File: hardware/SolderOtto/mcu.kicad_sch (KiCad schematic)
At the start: 30 parts, among them J301 TC-2050, P301 USB_C_Plug_USB2.0, SW301 SW_Push, U301 USBLC6-2SC6, U302 STM32G474QETx, U303 MX25R3235FM1xx0, Y301 32.768 kHz

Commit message: fix some part numbers
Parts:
- C317, C318: Digikey (none) -> 311-1636-1-ND
- R301, R302: Digikey (none) -> RMCF0603ZT0R00CT-ND
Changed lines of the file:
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@@
+			)
+		)
+		(property "Digikey" "311-1636-1-ND"
+			(at 304.8 232.41 0)
+			(effects
+				(font
+					(size 1.27 1.27)
+				)
+				(hide yes)
 			)
 		)
@@
 			)
 		)
+		(property "Digikey" "RMCF0603ZT0R00CT-ND"
+			(at 67.31 69.85 90)
+			(effects
+				(font
+					(size 1.27 1.27)
+				)
+				(hide yes)
+			)
+		)
 		(pin "1"
 		)
@@
 			)
 		)
+		(property "Digikey" "311-1636-1-ND"
+			(at 288.29 232.41 0)
+			(effects
+				(font
+					(size 1.27 1.27)
+				)
+				(hide yes)
+			)
+		)
 		(pin "1"
 		)
@@
 			(effects
 				(font
+					(size 1.27 1.27)
+				)
+				(hide yes)
+			)
+		)
+		(property "Digikey" "RMCF0603ZT0R00CT-ND"
+			(at 67.31 67.31 90)
+			(effects
+				(font

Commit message: remove low side switching ic
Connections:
- net Channel0_LOW_SIDE_COM: now reaches U302.32 (PA3)
- net Channel0_LOW_SIDE_SW renamed Channel0_LOW_SIDE_LOAD
- no-connect marks 17 -> 16
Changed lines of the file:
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@@
 	)
 	(no_connect
-		(at 212.09 67.31)
-	)
-	(no_connect
 		(at 161.29 107.95)
 	)
@@
 	(wire
 		(pts
+			(xy 212.09 67.31) (xy 228.6 67.31)
+		)
+		(stroke
+			(width 0)
+			(type default)
+		)
+	)
+	(wire
+		(pts
 			(xy 189.23 232.41) (xy 189.23 234.95)
 		)
@@
 		)
 	)
-	(hierarchical_label "Channel0_LOW_SIDE_SW"
+	(hierarchical_label "Channel0_LOW_SIDE_LOAD"
 		(shape output)
 		(at 143.51 102.87 180)
@@
 		)
 	)
+	(hierarchical_label "Channel0_LOW_SIDE_COM"
+		(shape output)
+		(at 228.6 67.31 0)
+		(fields_autoplaced yes)
+		(effects
+			(font
+				(size 1.27 1.27)
+			)
+			(justify left)
+		)
+	)

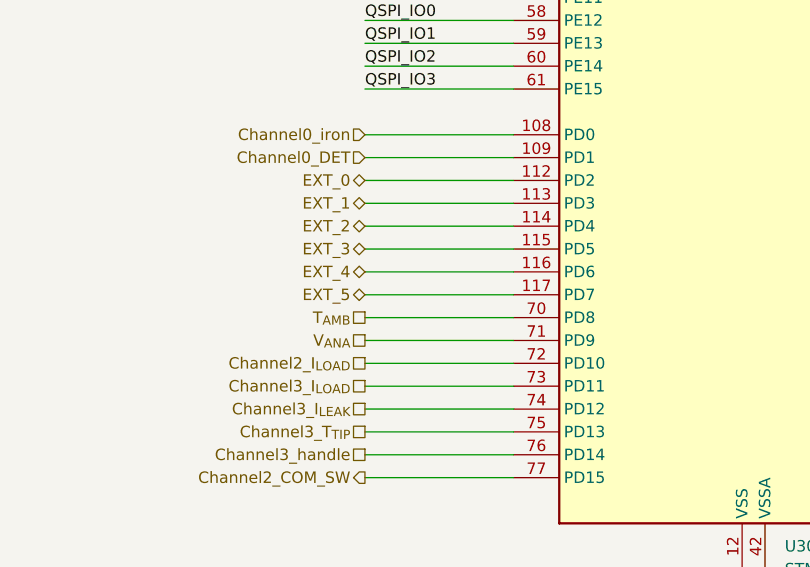
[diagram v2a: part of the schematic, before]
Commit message: rework pcb due to not working one
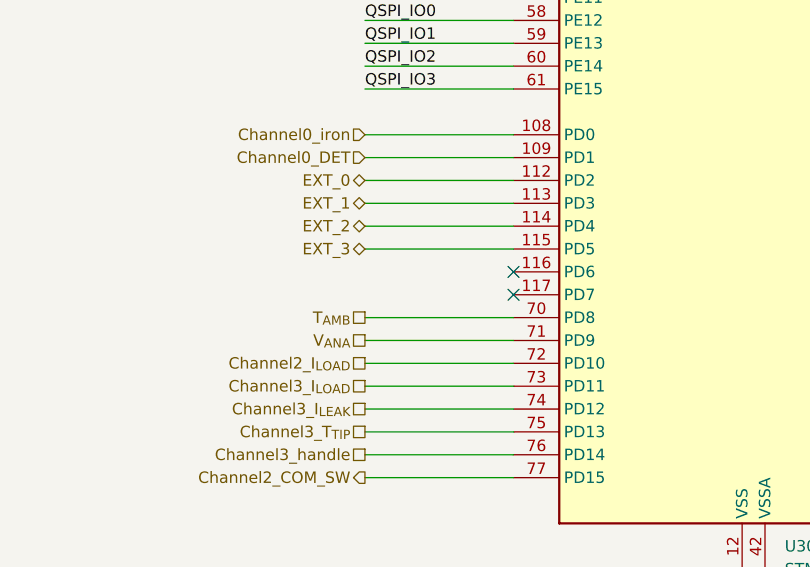
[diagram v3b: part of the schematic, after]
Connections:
- net EXT_4: no longer names the net of U302.116 (PD6)
- net EXT_5: no longer names the net of U302.117 (PD7)
- no-connect marks 16 -> 18
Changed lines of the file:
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@@
 	)
 	(no_connect
+		(at 161.29 199.39)
+	)
+	(no_connect
 		(at 212.09 176.53)
 	)
@@
 		(at 53.34 248.92)
 	)
+	(no_connect
+		(at 161.29 201.93)
+	)
 	(wire
 		(pts
@@
 	(wire
 		(pts
-			(xy 144.78 201.93) (xy 161.29 201.93)
-		)
-		(stroke
-			(width 0)
-			(type default)
-		)
-	)
-	(wire
-		(pts
 			(xy 144.78 118.11) (xy 161.29 118.11)
 		)
@@
 	(wire
 		(pts
-			(xy 144.78 199.39) (xy 161.29 199.39)
-		)
-		(stroke
-			(width 0)
-			(type default)
-		)
-	)
-	(wire
-		(pts
 			(xy 378.46 76.2) (xy 378.46 78.74)
 		)
@@
 		)
 	)
-	(hierarchical_label "EXT_5"
-		(shape bidirectional)
-		(at 144.78 201.93 180)
-		(fields_autoplaced yes)
-		(effects
-			(font
-				(size 1.27 1.27)
-			)
-			(justify right)
-		)
-	)
 	(hierarchical_label "Channel2_handle"
 		(shape passive)
@@
 		)
 	)
-	(hierarchical_label "EXT_4"
-		(shape bidirectional)
-		(at 144.78 199.39 180)
-		(fields_autoplaced yes)
-		(effects
-			(font
-				(size 1.27 1.27)
-			)
-			(justify right)
-		)
-	)

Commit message: rework pcb
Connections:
- net Channel3_SEL1 is gone; now on net ZCD: U302.83 (PG1)
- net Buzzer: now also U302.97 (PF6); no longer U302.7 (PC13)
- net Channel0_COM_SW: now also U302.14 (PF5); no longer U302.27 (PA0)
- net Channel0_I_{LEAK}: now also U302.27 (PA0); no longer U302.25 (PC3)
- net Channel0_LOAD0_SW: now also U302.7 (PC13); no longer U302.28 (PA1)
- net Channel0_LOAD1_SW: now also U302.11 (PF4); no longer U302.29 (PA2)
- net Channel0_LOW_SIDE_COM: now also U302.10 (PF3); no longer U302.32 (PA3)
- net Channel0_LOW_SIDE_LOAD: now also U302.15 (PF7); no longer U302.26 (PF2)
- net Channel0_iron: now also U302.36 (PA7); no longer U302.108 (PD0)
- net Channel0_stand: now also U302.35 (PA6); no longer U302.66 (PB12)
- net Channel0_tip: now also U302.34 (PA5); no longer U302.103 (PG5)
- net Channel1_COM_SW: no longer U302.41 (PB2)
- net Channel1_I_{LEAK}: no longer U302.35 (PA6)
- net Channel1_I_{LOAD}: no longer U302.36 (PA7)
- net Channel1_LOAD0_SW: no longer U302.39 (PB0)
- net Channel1_LOAD1_SW: no longer U302.40 (PB1)
- net Channel1_LOW_SIDE_SW: no longer U302.38 (PC5)
- net Channel1_T_{TIP}: no longer U302.34 (PA5)
- net Channel1_handle: no longer U302.33 (PA4)
- net Channel1_iron: no longer U302.119 (PB4)
- net Channel1_stand: no longer U302.67 (PB13)
- net Channel1_tip: no longer U302.104 (PG6)
- net Channel2_COM_SW: no longer U302.77 (PD15)
- net Channel2_I_{LEAK}: no longer U302.53 (PE7)
- net Channel2_I_{LOAD}: no longer U302.72 (PD10)
- net Channel2_LOAD0_SW: no longer U302.80 (PC6)
- net Channel2_LOAD1_SW: no longer U302.81 (PC7)
- net Channel2_LOW_SIDE_SW: no longer U302.82 (PG0)
- net Channel2_T_{TIP}: no longer U302.54 (PE8)
- net Channel2_handle: no longer U302.55 (PE9)
- net Channel2_iron: no longer U302.120 (PB5)
- net Channel2_stand: no longer U302.68 (PB14)
- net Channel2_tip: no longer U302.105 (PG7)
- net Channel3_COM_SW: no longer U302.86 (PG4)
- net Channel3_I_{LEAK}: no longer U302.74 (PD12)
- net Channel3_I_{LOAD}: no longer U302.73 (PD11)
- net Channel3_LOAD0_SW: no longer U302.87 (PC8)
- net Channel3_LOAD1_SW: no longer U302.88 (PC9)
- net Channel3_LOW_SIDE_SW: no longer U302.89 (PA8)
- net Channel3_T_{TIP}: no longer U302.75 (PD13)
- net Channel3_handle: no longer U302.76 (PD14)
- net Channel3_iron: no longer U302.122 (PB7)
- net Channel3_stand: no longer U302.69 (PB15)
- net Channel3_tip: no longer U302.106 (PG8)
- net EXT_0: now also U302.99 (PA15); no longer U302.112 (PD2)
- net EXT_1: now also U302.100 (PC10); no longer U302.113 (PD3)
- net EXT_2: now also U302.101 (PC11); no longer U302.114 (PD4)
- net EXT_3: now also U302.102 (PC12); no longer U302.115 (PD5)
- net ZCD: no longer U302.125 (PE0)
- net Channel0_SEL2_{b}: now reaches U302.19 (PF0)
- net Channel0_DET: no longer names the net of U302.109 (PD1)
- net Channel0_SEL1 renamed Channel0_SEL1_{a}
- net Channel0_SEL2 renamed Channel0_SEL1_{b}
- net Channel0_SEL3 renamed Channel0_SEL2_{a}
- net Channel0_T_{TIP} renamed Channel0_T_{TIP}_{a}
- net Channel1_DET: no longer names the net of U302.107 (PG9)
- net Channel1_SEL1: no longer names the net of U302.48 (PF11)
- net Channel1_SEL2: no longer names the net of U302.49 (PF12)
- net Channel1_SEL3: no longer names the net of U302.50 (PF13)
- net Channel2_DET: no longer names the net of U302.121 (PB6)
- net Channel2_SEL1: no longer names the net of U302.62 (PB10)
- net Channel2_SEL2: no longer names the net of U302.65 (PB11)
- net Channel2_SEL3: no longer names the net of U302.52 (PF15)
- net Channel3_DET: no longer names the net of U302.124 (PB9)
- net Channel3_SEL2: no longer names the net of U302.84 (PG2)
- net Channel3_SEL3: no longer names the net of U302.85 (PG3)
- new net Channel0_T_{TIP}_{b}: U302.25 (PC3)
- no-connect marks 18 -> 60

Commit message: save work
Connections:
- net Channel0_COM_SW: now also U302.7 (PC13); no longer U302.14 (PF5)
- net Channel0_LOAD0_SW: now also U302.10 (PF3); no longer U302.7 (PC13)
- net Channel0_LOW_SIDE_COM: now also U302.14 (PF5); no longer U302.10 (PF3)
- net Channel0_T_{TIP}_{a}: now also U302.25 (PC3); no longer U302.24 (PC2)
- net Channel0_T_{TIP}_{b}: now also U302.24 (PC2); no longer U302.25 (PC3)
- net ZCD: now also U302.39 (PB0); no longer U302.83 (PG1)
- net Channel0_iron: no longer names the net of U302.36 (PA7)
- no-connect marks 60 -> 63
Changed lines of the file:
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@@
 	)
 	(no_connect
+		(at 212.09 77.47)
+	)
+	(no_connect
 		(at 144.78 184.15)
 	)
@@
 	)
 	(no_connect
+		(at 161.29 102.87)
+	)
+	(no_connect
 		(at 228.6 67.31)
 	)
@@
 	)
 	(no_connect
+		(at 161.29 100.33)
+	)
+	(no_connect
 		(at 143.51 133.35)
 	)
@@
 	)
 	(no_connect
-		(at 143.51 67.31)
+		(at 143.51 69.85)
 	)
 	(no_connect
@@
 	)
 	(no_connect
-		(at 228.6 102.87)
+		(at 143.51 67.31)
 	)
 	(no_connect
@@
 	(wire
 		(pts
-			(xy 212.09 77.47) (xy 228.6 77.47)
-		)
-		(stroke
-			(width 0)
-			(type default)
-		)
-	)
-	(wire
-		(pts
 			(xy 143.51 97.79) (xy 161.29 97.79)
 		)
@@
 	(hierarchical_label "Channel0_LOAD0_SW"
 		(shape output)
-		(at 228.6 179.07 0)
+		(at 143.51 105.41 180)
 		(fields_autoplaced yes)
 		(effects
@@
 				(size 1.27 1.27)
 			)
-			(justify left)
+			(justify right)
 		)
 	)
@@
 	(hierarchical_label "Channel0_T_{TIP}_{b}"
 		(shape passive)
-		(at 228.6 153.67 0)
+		(at 228.6 151.13 0)
 		(fields_autoplaced yes)
 		(effects
@@
 	(hierarchical_label "Channel0_COM_SW"
 		(shape output)
-		(at 143.51 110.49 180)
+		(at 228.6 179.07 0)
 		(fields_autoplaced yes)
 		(effects
@@
 				(size 1.27 1.27)
 			)
-			(justify right)
+			(justify left)
 		)
 	)
@@
 		)
 	)
-	(hierarchical_label "Channel0_iron"
-		(shape input)
-		(at 228.6 77.47 0)
-		(fields_autoplaced yes)
-		(effects
-			(font
-				(size 1.27 1.27)
-			)
-			(justify left)
-		)
-	)
 	(hierarchical_label "Channel2_SEL2_{b}"
 		(shape output)
@@
 	(hierarchical_label "ZCD"
 		(shape input)
-		(at 143.51 69.85 180)
+		(at 228.6 102.87 0)
 		(fields_autoplaced yes)
 		(effects
@@
 				(size 1.27 1.27)
 			)
-			(justify right)
+			(justify left)
 		)
 	)
@@
 	(hierarchical_label "Channel0_T_{TIP}_{a}"
 		(shape passive)
-		(at 228.6 151.13 0)
+		(at 228.6 153.67 0)
 		(fields_autoplaced yes)
 		(effects
@@
 	(hierarchical_label "Channel0_LOW_SIDE_COM"
 		(shape output)
-		(at 143.51 105.41 180)
+		(at 143.51 110.49 180)
 		(fields_autoplaced yes)
 		(effects

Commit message: save work
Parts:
- added U304: STM32G474RETx, Package_QFP:LQFP-64_10x10mm_P0.5mm, symbol MCU_ST_STM32G4:STM32G474RETx
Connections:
- new net: U304.15 (VSS), U304.31 (VSS), U304.47 (VSS), U304.63 (VSS)
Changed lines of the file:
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@@
+	)
+	(symbol
+		(lib_id "MCU_ST_STM32G4:STM32G474RETx")
+		(at 100.33 187.96 0)
+		(unit 1)
+		(exclude_from_sim no)
+		(in_bom yes)
+		(on_board yes)
+		(dnp no)
+		(fields_autoplaced yes)
+		(property "Reference" "U304"
+			(at 105.0641 236.22 0)
+			(effects
+				(font
+					(size 1.27 1.27)
+				)
+				(justify left)
+			)
+		)
+		(property "Value" "STM32G474RETx"
+			(at 105.0641 238.76 0)
+			(effects
+				(font
+					(size 1.27 1.27)
+				)
+				(justify left)
+			)
+		)
+		(property "Footprint" "Package_QFP:LQFP-64_10x10mm_P0.5mm"
+			(at 85.09 233.68 0)
+			(effects
+				(font
+					(size 1.27 1.27)
+				)
+				(justify right)
+				(hide yes)
+			)
+		)
+		(property "Datasheet" "https://www.st.com/resource/en/datasheet/stm32g474re.pdf"
+			(at 100.33 187.96 0)
+			(effects
+				(font
+					(size 1.27 1.27)
+				)
+				(hide yes)
+			)
+		)
+		(property "Description" "STMicroelectronics Arm Cortex-M4 MCU, 512KB flash, 128KB RAM, 170 MHz, 1.71-3.6V, 52 GPIO, LQFP64"
+			(at 100.33 187.96 0)
+			(effects
+				(font
+					(size 1.27 1.27)
+				)
+				(hide yes)
+			)
+		)
+		(pin "41"
+		)
+		(pin "50"
+		)
+		(pin "5"
+		)
+		(pin "53"
+		)
+		(pin "12"
+		)
+		(pin "58"
+		)
+		(pin "33"
+		)
+		(pin "47"
+		)
+		(pin "35"
+		)
+		(pin "59"
+		)
+		(pin "23"
+		)
+		(pin "61"
+		)
+		(pin "15"
+		)
+		(pin "51"
+		)
+		(pin "54"
+		)
+		(pin "28"
+		)
+		(pin "7"
+		)
+		(pin "38"
+		)
+		(pin "37"
+		)
+		(pin "36"
+		)
+		(pin "43"
+		)
+		(pin "44"
+		)
+		(pin "6"
+		)
+		(pin "19"
+		)
+		(pin "48"
+		)
+		(pin "31"
+		)
+		(pin "21"
+		)
+		(pin "39"
+		)
+		(pin "63"
+		)
+		(pin "4"
+		)
+		(pin "16"
+		)
+		(pin "49"
+		)
+		(pin "11"
+		)
+		(pin "2"
+		)
+		(pin "20"
+		)
+		(pin "56"
+		)
+		(pin "57"
+		)
+		(pin "55"
+		)
+		(pin "60"
+		)
+		(pin "18"
+		)
+		(pin "40"
+		)
+		(pin "26"
+		)
+		(pin "30"
+		)
+		(pin "34"
+		)
+		(pin "52"
+		)
+		(pin "17"
+		)
+		(pin "32"
+		)
+		(pin "64"
+		)
+		(pin "42"
+		)
+		(pin "24"
+		)
+		(pin "29"
+		)
+		(pin "45"
+		)
+		(pin "14"
+		)
+		(pin "13"
+		)
+		(pin "9"
+		)
+		(pin "22"
+		)
+		(pin "8"
+		)
+		(pin "27"
+		)
+		(pin "25"
+		)
+		(pin "10"
+		)
+		(pin "1"
+		)
+		(pin "46"
+		)
+		(pin "62"
+		)
+		(pin "3"
+		)
+		(instances
+			(project ""
+				(path "/04e99464-bf33-4a4f-8397-d26b5ec904f3/884179ac-e5b2-4774-935d-cb1e08eb2d75"
+					(reference "U304")
+					(unit 1)
+				)
+			)
+		)
 	)
 	(symbol

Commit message: rework schematic foir single channel
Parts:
- removed C306, C307, C308, C310: 100n, Resistor_SMD:R_0402_1005Metric, symbol Device:C
- removed U302: STM32G474QETx, Package_QFP:LQFP-128_14x14mm_P0.4mm, symbol MCU_ST_STM32G4:STM32G474QETx
- renumbered C309 to C306, C311 to C307, C312 to C308, C313 to C309, C314 to C310, C315 to C311, C316 to C312, C317 to C313, C318 to C314, C319 to C315, U304 to U302
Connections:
- net +3V3: now also U302.1 (VBAT), U302.16 (VDD), U302.32 (VDD), U302.48 (VDD), U302.64 (VDD)
- net Buzzer: now also U302.62 (PB9)
- net Channel0_I_{LEAK}: now also U302.17 (PA3)
- net Channel0_I_{LOAD}: now also U302.14 (PA2)
- net Channel0_SEL1_{a}: now also U302.37 (PB15)
- net Channel0_SEL1_{b}: now also U302.36 (PB14)
- net Channel0_SEL2_{a}: now also U302.35 (PB13)
- net Channel0_SEL2_{b}: now also U302.34 (PB12)
- net Channel0_T_{TIP}_{a}: now also U302.12 (PA0)
- net Channel0_T_{TIP}_{b}: now also U302.13 (PA1)
- net Channel0_handle: now also U302.11 (PC3)
- net Channel0_stand: now also U302.9 (PC1)
- net Channel0_tip: now also U302.10 (PC2)
- net D+: now also U302.46 (PA12)
- net D-: now also U302.45 (PA11)
- net DBG_RX: now also U302.44 (PA10)
- net DBG_TX: now also U302.43 (PA9)
- net DISP_CLK: now also U302.52 (PC10)
- net DISP_INT: now also U302.55 (PD2)
- net DISP_MISO: now also U302.53 (PC11)
- net DISP_MOSI: now also U302.54 (PC12)
- net DISP_NSS: now also U302.51 (PA15)
- net DISP_~{PD}: now also U302.57 (PB4)
- net EXT_0: now also U302.41 (PC9)
- net EXT_1: now also U302.40 (PC8)
- net EXT_2: now also U302.39 (PC7)
- net EXT_3: now also U302.38 (PC6)
- net GND: now also U302.15 (VSS), U302.27 (VSSA), U302.31 (VSS), U302.47 (VSS), U302.61 (PB8), U302.63 (VSS)
- net LSE_IN: now also U302.6 (PF1)
- net LSE_OUT: now also U302.5 (PF0)
- net QSPI_CLK: now also U302.30 (PB10)
- net QSPI_IO0: now also U302.25 (PB1)
- net QSPI_IO1: now also U302.24 (PB0)
- net QSPI_IO2: now also U302.21 (PA7)
- net QSPI_IO3: now also U302.20 (PA6)
- net QSPI_NCS: now also U302.33 (PB11)
- net SWDCLK: now also U302.50 (PA14)
- net SWDIO: now also U302.49 (PA13)
- net SWO: now also U302.56 (PB3)
- net T_{AMB}: now also U302.26 (PB2)
- net VDDA: now also U302.28 (VREF+), U302.29 (VDDA)
- net V_{ANA}: now also U302.23 (PC5)
- net ZCD: now also U302.8 (PC0)
- net ~{RESET}: now also U302.7 (PG10)
- net Channel0_LOAD0: now reaches U302.2 (PC13)
- net Channel0_LOAD1: now reaches U302.3 (PC14)
- no-connect marks 63 -> 10
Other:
- moved on the sheet: C301, C302, C303, C304, C305, C306, U302

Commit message: save shit
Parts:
- removed J301: TC-2050, mylib_connector:TC-2050, symbol mylib_connectors:TC-2050
- removed R301, R302: 0, Resistor_SMD:R_0603_1608Metric, symbol Device:R
- added J302: Conn_ARM_SWD_TagConnect_TC2030, Connector:Tag-Connect_TC2030-IDC-FP_2x03_P1.27mm_Vertical, symbol Connector:Conn_ARM_SWD_TagConnect_TC2030
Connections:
- net +3V3: now also J302.1 (VCC)
- net Buzzer: now also U302.14 (PA2); no longer U302.62 (PB9)
- net Channel0_I_{LEAK}: now also U302.13 (PA1); no longer U302.17 (PA3)
- net Channel0_I_{LOAD}: now also U302.9 (PC1); no longer U302.14 (PA2)
- net Channel0_SEL1_{a}: now also U302.58 (PB5); no longer U302.37 (PB15)
- net Channel0_SEL1_{b}: now also U302.60 (PB7); no longer U302.36 (PB14)
- net Channel0_SEL2_{a}: now also U302.59 (PB6); no longer U302.35 (PB13)
- net Channel0_SEL2_{b}: now also U302.62 (PB9); no longer U302.34 (PB12)
- net Channel0_T_{TIP}_{a}: now also U302.10 (PC2); no longer U302.12 (PA0)
- net Channel0_T_{TIP}_{b}: now also U302.11 (PC3); no longer U302.13 (PA1)
- net Channel0_handle: now also U302.12 (PA0); no longer U302.11 (PC3)
- net Channel0_stand: now also U302.18 (PA4); no longer U302.9 (PC1)
- net Channel0_tip: now also U302.17 (PA3); no longer U302.10 (PC2)
- net GND: now also J302.5 (GND)
- net SWDCLK: now also J302.4 (SWCLK)
- net SWDIO: now also J302.2 (SWDIO)
- net SWO: now also J302.6 (SWO)
- net T_{AMB}: now also U302.34 (PB12); no longer U302.26 (PB2)
- net V_{ANA}: now also U302.35 (PB13); no longer U302.23 (PC5)
- net ~{RESET}: now also J302.3 (~{RESET})
- net Channel0_det: now reaches U302.19 (PA5)
- net DBG_RX: no longer names the net of U302.44 (PA10)
- net DBG_TX: no longer names the net of U302.43 (PA9)
- no-connect marks 10 -> 13
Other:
- moved on the sheet: C315, SW301, U302
